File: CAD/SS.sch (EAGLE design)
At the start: 82 parts, among them Q1 SN74AHC-OR, Q2 UMD5N, Q4 SN74AHC-OR, Q5 BFP460, Q6 L78L05, Q7 NCP553, T1 MMBTRA104SS

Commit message: Board: Pouring some copper over it
Started designing the board layout.
Plus, schematic: Fixed an error on 100R relay resistor placement
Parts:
- removed C3: 27pF, aarf:MURATACAP
- removed C4, C5: 6.8pF, aarf:MURATACAP
- added L10, L11: 5.6nH, aarf:L-0805
- added L9: 56nH, aarf:L-0805
- C6: value 43pF -> 27pF
- C7: value 4.7pF -> 27pF
- L6: value 27nH -> 56nH
- L8: value 27nH -> 150nH
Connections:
- removed net N$19: C5.1, C6.2, L8.2
- removed net N$20: C5.2, L6.1
- removed net N$30: R10.2, RL2.1
- new net N$11: C7.2, L11.1, L6.1, L8.2
- new net N$8: C6.2, L10.1, L8.1, L9.2
- net GND: now also L10.2, L11.2; no longer C3.1
- net N$1: now also C17.2, D2.C
- net N$18: now also C18.1, D3.C, R10.1, RL2.1; no longer C4.2, L8.1
- net N$21: no longer C7.2
- net N$4: now also L9.1; no longer C3.2, C4.1
- net RELAY_PWR: now also R10.2; no longer C17.2, C18.1, D2.C, D3.C, R10.1
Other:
- moved on the sheet: C17, C6, C7, D2, L6, L8, R10, R9, RL1

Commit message: More copper poured
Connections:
- net N$21 renamed UHF-OUT
- net N$3 renamed VHF-IN
- net N$4 renamed UHF-IN
- net N$7 renamed VHF-OUT
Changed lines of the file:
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@@
 </segment>
 </net>
-<net name="N$21" class="0">
+<net name="UHF-OUT" class="0">
 <segment>
 <pinref part="L6" gate="G$1" pin="2"/>
@@
 </segment>
 </net>
-<net name="N$4" class="0">
+<net name="UHF-IN" class="0">
 <segment>
 <pinref part="SW_SEL_V/U-IN" gate="G$1" pin="RF2"/>
@@
 </segment>
 </net>
-<net name="N$7" class="0">
+<net name="VHF-OUT" class="0">
 <segment>
 <pinref part="SW_SEL_V/U-OUT" gate="G$1" pin="RF1"/>
@@
 </segment>
 </net>
-<net name="N$3" class="0">
+<net name="VHF-IN" class="0">
 <segment>
 <pinref part="L1" gate="G$1" pin="1"/>

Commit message: Progress
- Replaced capacitors and resistors with ones who has a PCB marking
- Poured more copper
- Added annotations
- Some block relocations
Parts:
- C13, C14, C15, C16, C17, C18, C19, C20, C21, C22, C23, C24: device rcl:C-EUC0805 -> aarf:C-0805
- R1, R10, R11, R12, R13, R14, R2, R3, R4, R5, R6, R7, R8, R9: device rcl:R-US_M1206 -> aarf:R-1206
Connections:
- net N$6 renamed IN_DECPL
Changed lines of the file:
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@@
 <part name="C7" library="aarf" deviceset="MURATACAP" device="" value="27pF"/>
 <part name="C8" library="aarf" deviceset="MURATACAP" device="" value="390pF"/>
-<part name="R1" library="rcl" library_urn="urn:adsk.eagle:library:334" deviceset="R-US_" device="M1206" package3d_urn="urn:adsk.eagle:package:23566/1" value="82kΩ"/>
-<part name="R2" library="rcl" library_urn="urn:adsk.eagle:library:334" deviceset="R-US_" device="M1206" package3d_urn="urn:adsk.eagle:package:23566/1" value="430Ω"/>
+<part name="R1" library="aarf" deviceset="R-1206" device="" value="82kΩ"/>
+<part name="R2" library="aarf" deviceset="R-1206" device="" value="430Ω"/>
 <part name="C9" library="aarf" deviceset="MURATACAP" device="" value="390pF"/>
-<part name="R3" library="rcl" library_urn="urn:adsk.eagle:library:334" deviceset="R-US_" device="M1206" package3d_urn="urn:adsk.eagle:package:23566/1" value="300Ω"/>
-<part name="R4" library="rcl" library_urn="urn:adsk.eagle:library:334" deviceset="R-US_" device="M1206" package3d_urn="urn:adsk.eagle:package:23566/1" value="130Ω"/>
+<part name="R3" library="aarf" deviceset="R-1206" device="" value="300Ω"/>
+<part name="R4" library="aarf" deviceset="R-1206" device="" value="130Ω"/>
 <part name="C10" library="aarf" deviceset="MURATACAP" device="" value="390pF"/>
 <part name="C11" library="aarf" deviceset="MURATACAP" device="" value="220nF"/>
@@
 </part>
 <part name="FB2" library="aarf" deviceset="FB-0805" device="" value="BLM21"/>
-<part name="R5" library="rcl" library_urn="urn:adsk.eagle:library:334" deviceset="R-US_" device="M1206" package3d_urn="urn:adsk.eagle:package:23566/1" value="10kΩ"/>
-<part name="C13" library="rcl" library_urn="urn:adsk.eagle:library:334" deviceset="C-EU" device="C0805" package3d_urn="urn:adsk.eagle:package:23617/2" value="0.001µ"/>
-<part name="C14" library="rcl" library_urn="urn:adsk.eagle:library:334" deviceset="C-EU" device="C0805" package3d_urn="urn:adsk.eagle:package:23617/2" value="0.001µ"/>
+<part name="R5" library="aarf" deviceset="R-1206" device="" value="10kΩ"/>
+<part name="C13" library="aarf" deviceset="C-0805" device="" value="0.001µ"/>
+<part name="C14" library="aarf" deviceset="C-0805" device="" value="0.001µ"/>
 <part name="X_8" library="ngspice-simulation" library_urn="urn:adsk.eagle:library:527439" deviceset="GND" device=""/>
-<part name="R6" library="rcl" library_urn="urn:adsk.eagle:library:334" deviceset="R-US_" device="M1206" package3d_urn="urn:adsk.eagle:package:23566/1" value="10kΩ"/>
+<part name="R6" library="aarf" deviceset="R-1206" device="" value="10kΩ"/>
 <part name="FB3" library="aarf" deviceset="FB-0805" device="" value="BLM21"/>
-<part name="C15" library="rcl" library_urn="urn:adsk.eagle:library:334" deviceset="C-EU" device="C0805" package3d_urn="urn:adsk.eagle:package:23617/2" value="0.001µ"/>
+<part name="C15" library="aarf" deviceset="C-0805" device="" value="0.001µ"/>
 <part name="Q1" library="aarf" deviceset="SN74AHC-OR" device="" package3d_urn="urn:adsk.eagle:package:2405/1"/>
-<part name="C16" library="rcl" library_urn="urn:adsk.eagle:library:334" deviceset="C-EU" device="C0805" package3d_urn="urn:adsk.eagle:package:23617/2" value="0.001µ"/>
+<part name="C16" library="aarf" deviceset="C-0805" device="" value="0.001µ"/>
 <part name="BYPASS" library="wirepad" library_urn="urn:adsk.eagle:library:412" deviceset="SMD2" device="" package3d_urn="urn:adsk.eagle:package:30839/1" value="BYPASS"/>
-<part name="R7" library="rcl" library_urn="urn:adsk.eagle:library:334" deviceset="R-US_" device="M1206" package3d_urn="urn:adsk.eagle:package:23566/1" value="10kΩ"/>
+<part name="R7" library="aarf" deviceset="R-1206" device="" value="10kΩ"/>
 <part name="FB4" library="aarf" deviceset="FB-0805" device="" value="BLM21"/>
 <part name="Q2" library="aarf" deviceset="UMD5N" device="" value="UMD5N"/>
-<part name="R9" library="rcl" library_urn="urn:adsk.eagle:library:334" deviceset="R-US_" device="M1206" package3d_urn="urn:adsk.eagle:package:23566/1" value="100Ω"/>
+<part name="R9" library="aarf" deviceset="R-1206" device="" value="100Ω"/>
 <part name="D2" library="aarf" deviceset="D-SOD323" device="" value="1N4148"/>
-<part name="C17" library="rcl" library_urn="urn:adsk.eagle:library:334" deviceset="C-EU" device="C0805" package3d_urn="urn:adsk.eagle:package:23617/2" value="0.1µ"/>
+<part name="C17" library="aarf" deviceset="C-0805" device="" value="0.1µ"/>
 <part name="D3" library="aarf" deviceset="D-SOD323" device="" value="1N4148"/>
-<part name="C18" library="rcl" library_urn="urn:adsk.eagle:library:334" deviceset="C-EU" device="C0805" package3d_urn="urn:adsk.eagle:package:23617/2" value="0.1µ"/>
-<part name="R10" library="rcl" library_urn="urn:adsk.eagle:library:334" deviceset="R-US_" device="M1206" package3d_urn="urn:adsk.eagle:package:23566/1" value="100Ω"/>
-<part name="C19" library="rcl" library_urn="urn:adsk.eagle:library:334" deviceset="C-EU" device="C0805" package3d_urn="urn:adsk.eagle:package:23617/2" value="0.001µ"/>
+<part name="C18" library="aarf" deviceset="C-0805" device="" value="0.1µ"/>
+<part name="R10" library="aarf" deviceset="R-1206" device="" value="100Ω"/>
+<part name="C19" library="aarf" deviceset="C-0805" device="" value="0.001µ"/>
 <part name="UHF" library="wirepad" library_urn="urn:adsk.eagle:library:412" deviceset="SMD2" device="" package3d_urn="urn:adsk.eagle:package:30839/1" value="UHF"/>
-<part name="R11" library="rcl" library_urn="urn:adsk.eagle:library:334" deviceset="R-US_" device="M1206" package3d_urn="urn:adsk.eagle:package:23566/1" value="10kΩ"/>
+<part name="R11" library="aarf" deviceset="R-1206" device="" value="10kΩ"/>
 <part name="FB5" library="aarf" deviceset="FB-0805" device="" value="BLM21"/>
-<part name="C20" library="rcl" library_urn="urn:adsk.eagle:library:334" deviceset="C-EU" device="C0805" package3d_urn="urn:adsk.eagle:package:23617/2" value="0.001µ"/>
+<part name="C20" library="aarf" deviceset="C-0805" device="" value="0.001µ"/>
 <part name="AMP_OFF" library="wirepad" library_urn="urn:adsk.eagle:library:412" deviceset="SMD2" device="" package3d_urn="urn:adsk.eagle:package:30839/1" value="AMP_OFF"/>
-<part name="R12" library="rcl" library_urn="urn:adsk.eagle:library:334" deviceset="R-US_" device="M1206" package3d_urn="urn:adsk.eagle:package:23566/1" value="10kΩ"/>
+<part name="R12" library="aarf" deviceset="R-1206" device="" value="10kΩ"/>
 <part name="FB6" library="aarf" deviceset="FB-0805" device="" value="BLM21"/>
 <part name="Q4" library="aarf" deviceset="SN74AHC-OR" device="" package3d_urn="urn:adsk.eagle:package:2405/1"/>
-<part name="C21" library="rcl" library_urn="urn:adsk.eagle:library:334" deviceset="C-EU" device="C0805" package3d_urn="urn:adsk.eagle:package:23617/2" value="0.33µ"/>
-<part name="C22" library="rcl" library_urn="urn:adsk.eagle:library:334" deviceset="C-EU" device="C0805" package3d_urn="urn:adsk.eagle:package:23617/2" value="0.1µ"/>
+<part name="C21" library="aarf" deviceset="C-0805" device="" value="0.33µ"/>
+<part name="C22" library="aarf" deviceset="C-0805" device="" value="0.1µ"/>
 <part name="Q7" library="aarf" deviceset="NCP553" device=""/>
-<part name="C23" library="rcl" library_urn="urn:adsk.eagle:library:334" deviceset="C-EU" device="C0805" package3d_urn="urn:adsk.eagle:package:23617/2" value="1µ"/>
-<part name="C24" library="rcl" library_urn="urn:adsk.eagle:library:334" deviceset="C-EU" device="C0805" package3d_urn="urn:adsk.eagle:package:23617/2" value="0.33µ"/>
+<part name="C23" library="aarf" deviceset="C-0805" device="" value="1µ"/>
+<part name="C24" library="aarf" deviceset="C-0805" device="" value="0.33µ"/>
 <part name="Q6" library="aarf" deviceset="MIC5365" device="" value="L78L05"/>
 <part name="SW_ISOL-ANT" library="aarf" deviceset="PE4259" device="" value="PE4259"/>
@@
 <part name="RL2" library="aarf" deviceset="RELAY-TE-HF3" device="" value="RADIO_RLY"/>
 <part name="T1" library="transistor" library_urn="urn:adsk.eagle:library:402" deviceset="*-PNP_DRIVER-" device="SC59-BEC" package3d_urn="urn:adsk.eagle:package:28754/2" technology="MUN2111T1" value="MMBTRA104SS"/>
-<part name="R8" library="rcl" library_urn="urn:adsk.eagle:library:334" deviceset="R-US_" device="M1206" package3d_urn="urn:adsk.eagle:package:23566/1" value="1kΩ"/>
+<part name="R8" library="aarf" deviceset="R-1206" device="" value="1kΩ"/>
 <part name="L7" library="aarf" deviceset="L-0805" device="" value="1000µH"/>
-<part name="R13" library="rcl" library_urn="urn:adsk.eagle:library:334" deviceset="R-US_" device="M1206" package3d_urn="urn:adsk.eagle:package:23566/1" value="10kΩ"/>
-<part name="R14" library="rcl" library_urn="urn:adsk.eagle:library:334" deviceset="R-US_" device="M1206" package3d_urn="urn:adsk.eagle:package:23566/1" value="10kΩ"/>
+<part name="R13" library="aarf" deviceset="R-1206" device="" value="10kΩ"/>
+<part name="R14" library="aarf" deviceset="R-1206" device="" value="10kΩ"/>
 <part name="ANTENNA" library="wirepad" library_urn="urn:adsk.eagle:library:412" deviceset="SMD2" device="" package3d_urn="urn:adsk.eagle:package:30839/1" value="ANTENNA"/>
 <part name="RADIO" library="wirepad" library_urn="urn:adsk.eagle:library:412" deviceset="SMD2" device="" package3d_urn="urn:adsk.eagle:package:30839/1" value="RADIO"/>
@@
 </segment>
 </net>
-<net name="N$6" class="0">
+<net name="IN_DECPL" class="0">
 <segment>
 <pinref part="C25" gate="G$1" pin="2"/>
@@
 packages will not be understood (or retained) with this version.
 </note>
-<note version="8.4" severity="warning">
-Since Version 8.4, EAGLE supports properties for SPICE simulation.
-Probes in schematics and SPICE mapping objects found in parts and library devices
-will not be understood with this version. Update EAGLE to the latest version
-for full support of SPICE simulation.
-</note>
 </compatibility>

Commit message: More progress
- Featuring: CPWs (check https://resources.altium.com/p/pros-and-cons-of-different-high-frequency-transmission-line-types)
- Revamped BPF component layout
- Serious routing in RF side
- More labeled signals

Getting closer to the real deal
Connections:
- net N$1 renamed FEED-RA
- net N$18 renamed FEED-RB
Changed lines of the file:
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@@
 </segment>
 </net>
-<net name="N$18" class="0">
+<net name="FEED-RB" class="0">
 <segment>
 <wire x1="307.34" y1="228.6" x2="307.34" y2="243.84" width="0.1524" layer="91"/>
@@
 </segment>
 </net>
-<net name="N$1" class="0">
+<net name="FEED-RA" class="0">
 <segment>
 <pinref part="R9" gate="G$1" pin="2"/>

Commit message: Fixed crass error on LNA RF switch
it was flipped the ports RF1/RF2 (NO/NC)
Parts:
- VHF: value UHF -> VHF
- renumbered UHF to VHF
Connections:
- net SEL_BPF_UHF renamed SEL_BPF_VHF
- removed net LNA_BYPASS: SW_SEL_LNA-IN.RF2, SW_SEL_LNA-OUT.RF2
- removed net LNA_IN: C8.1, SW_SEL_LNA-IN.RF1
- removed net LNA_OUT: C12.2, SW_SEL_LNA-OUT.RF1
- new net LNA-BYPASS: SW_SEL_LNA-IN.NO, SW_SEL_LNA-OUT.NO
- new net N$1: C12.2, SW_SEL_LNA-OUT.NC
- new net N$4: C8.1, SW_SEL_LNA-IN.NC
- net BPF_IN: now also SW_ISOL-ANT.NC; no longer SW_ISOL-ANT.RF2
- net GND: now also SW_ISOL-ANT.NO, SW_ISOL-RADIO.NO; no longer SW_ISOL-ANT.RF1, SW_ISOL-RADIO.RF1
- net LNA-SW_OUT: now also SW_ISOL-RADIO.NC; no longer SW_ISOL-RADIO.RF2
- net UHF-IN: now also SW_SEL_V/U-IN.NC; no longer SW_SEL_V/U-IN.RF2
- net UHF-OUT: now also SW_SEL_V/U-OUT.NC; no longer SW_SEL_V/U-OUT.RF2
- net VHF-IN: now also SW_SEL_V/U-IN.NO; no longer SW_SEL_V/U-IN.RF1
- net VHF-OUT: now also SW_SEL_V/U-OUT.NO; no longer SW_SEL_V/U-OUT.RF1
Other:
- moved on the sheet: D4, SW_ISOL-RADIO, SW_SEL_LNA-IN, SW_SEL_LNA-OUT

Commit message: Fixed relay/switch logics
* REviewed thoroughly the relay logic and connectors.
* Had to add a new "NOR" part. Complexity wins...
* Re-routed 5V regulator Enable pin to LNA logic
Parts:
- AMP_ON: value AMP_OFF -> AMP_ON
- Q1: value SN74AHC-OR -> SN74AHC-NOR; device aarf:SN74AHC-OR -> aarf:SN74AHC-NOR
- Q4: value SN74AHC-OR -> SN74AHC-AND; device aarf:SN74AHC-OR -> aarf:SN74AHC-AND
- renumbered AMP_OFF to AMP_ON
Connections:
- net AMP_OFF renamed AMP_ON
- net EXT_BYPASS renamed FORCE_BYPASS
- net RELAY_PWR renamed RELAY-RX_ON
- removed net LNA_OFF: Q4.Y, SW_SEL_LNA-IN.CTRL, SW_SEL_LNA-OUT.CTRL
- removed net N$4: C8.1, SW_SEL_LNA-IN.NC
- removed net RLY_BYPASS: Q1.Y, Q2.5, Q4.A, Q6.EN, SW_ISOL-ANT.CTRL, SW_ISOL-RADIO.CTRL
- new net BPF_ON: Q1.Y, Q2.5, Q4.A, SW_ISOL-ANT.CTRL, SW_ISOL-RADIO.CTRL
- new net LNA_ON: Q4.Y, Q6.EN, SW_SEL_LNA-IN.CTRL, SW_SEL_LNA-OUT.CTRL
- new net N$3: C8.1, SW_SEL_LNA-IN.NO
- net BPF_IN: now also SW_ISOL-ANT.NO; no longer SW_ISOL-ANT.NC
- net GND: now also SW_ISOL-ANT.NC, SW_ISOL-RADIO.NC; no longer SW_ISOL-ANT.NO, SW_ISOL-RADIO.NO
- net LNA-BYPASS: now also SW_SEL_LNA-IN.NC, SW_SEL_LNA-OUT.NC; no longer SW_SEL_LNA-IN.NO, SW_SEL_LNA-OUT.NO
- net LNA-SW_OUT: now also SW_ISOL-RADIO.NO; no longer SW_ISOL-RADIO.NC
- net N$1: now also SW_SEL_LNA-OUT.NO; no longer SW_SEL_LNA-OUT.NC
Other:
- note added: "LNA CONTROL"
- note removed: "LNA CONTROL ON/BYP"
- moved on the sheet: SW_SEL_LNA-IN, SW_SEL_LNA-OUT

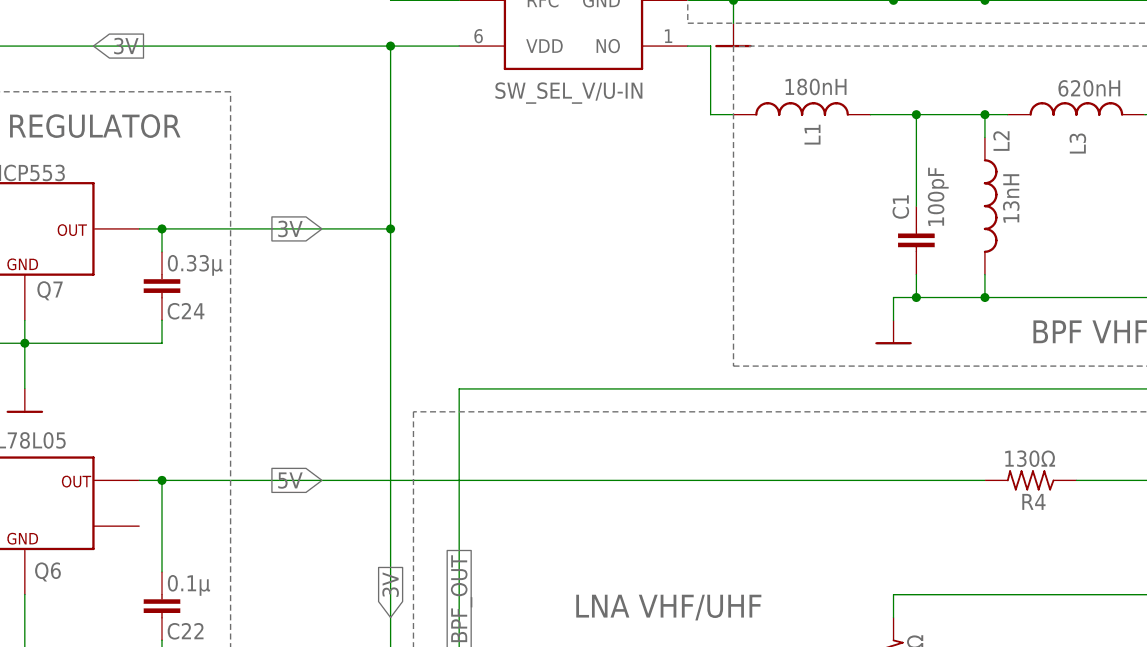
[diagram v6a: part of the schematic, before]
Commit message: Updates to Board & Schematics
Schematic: 
* Added pads for 3V and 5V
Board:
* Added signal direction on signal pads
* Added a lot of gimmicks
* Added exposed copper so I can try the effects of covering some RF-critical sections with copper tape
* Reviewed some component position
* More comments
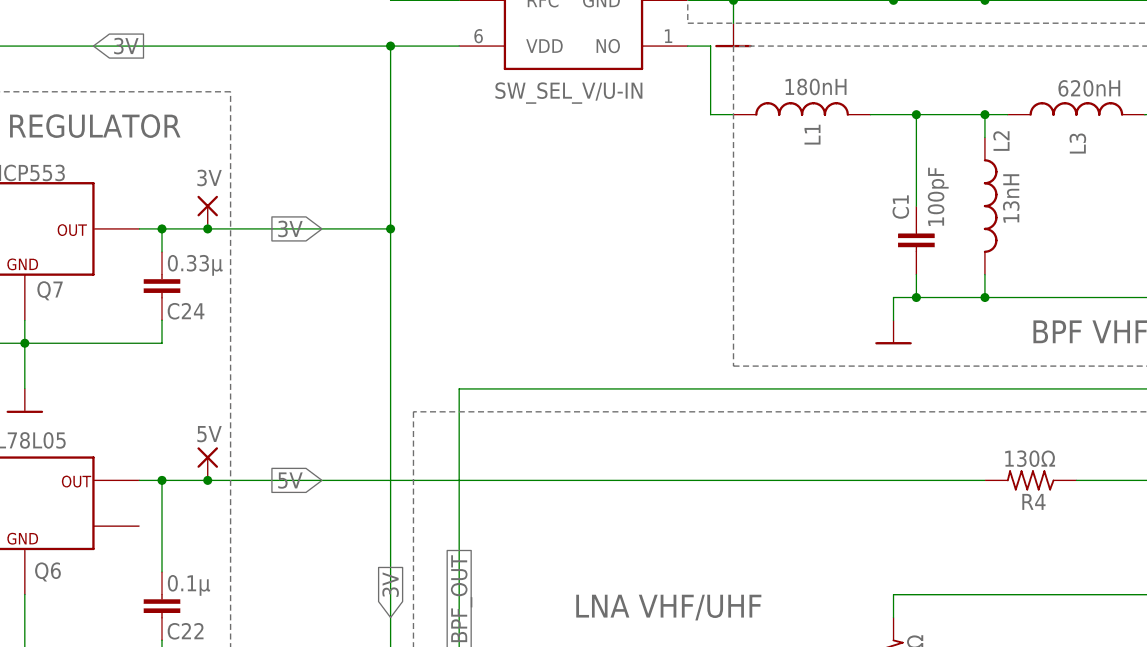
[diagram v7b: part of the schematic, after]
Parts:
- added 3V: 3V, wirepad:SMD2
- added 5V: 5V, wirepad:SMD2
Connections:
- net 3V: now also 3V.P
- net 5V: now also 5V.P
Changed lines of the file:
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@@
 <part name="GND16" library="supply1" library_urn="urn:adsk.eagle:library:371" deviceset="GND" device=""/>
 <part name="GND18" library="supply1" library_urn="urn:adsk.eagle:library:371" deviceset="GND" device=""/>
+<part name="5V" library="wirepad" library_urn="urn:adsk.eagle:library:412" deviceset="SMD2" device="" package3d_urn="urn:adsk.eagle:package:30839/1" value="5V"/>
+<part name="3V" library="wirepad" library_urn="urn:adsk.eagle:library:412" deviceset="SMD2" device="" package3d_urn="urn:adsk.eagle:package:30839/1" value="3V"/>
 </parts>
 <sheets>
@@
 <instance part="GND16" gate="1" x="281.94" y="58.42" smashed="yes"/>
 <instance part="GND18" gate="1" x="210.82" y="58.42" smashed="yes"/>
+<instance part="5V" gate="1" x="149.86" y="114.3" smashed="yes" rot="R270">
+<attribute name="NAME" x="149.987" y="116.9162" size="1.778" layer="95" align="center"/>
+</instance>
+<instance part="3V" gate="1" x="149.86" y="142.24" smashed="yes" rot="R270">
+<attribute name="NAME" x="149.987" y="145.3642" size="1.778" layer="95" align="center"/>
+</instance>
 </instances>
 <busses>
@@
 <pinref part="C22" gate="G$1" pin="2"/>
 <wire x1="144.78" y1="111.76" x2="144.78" y2="101.6" width="0.1524" layer="91"/>
-<wire x1="144.78" y1="111.76" x2="236.22" y2="111.76" width="0.1524" layer="91"/>
+<wire x1="144.78" y1="111.76" x2="149.86" y2="111.76" width="0.1524" layer="91"/>
 <junction x="144.78" y="111.76"/>
 <pinref part="R4" gate="G$1" pin="2"/>
 <label x="162.56" y="111.76" size="1.778" layer="255" rot="R180" xref="yes"/>
 <pinref part="Q6" gate="G$1" pin="VOUT"/>
+<pinref part="5V" gate="1" pin="P"/>
+<wire x1="149.86" y1="111.76" x2="236.22" y2="111.76" width="0.1524" layer="91"/>
+<junction x="149.86" y="111.76"/>
 </segment>
 </net>
@@
 <wire x1="170.18" y1="160.02" x2="119.38" y2="160.02" width="0.1524" layer="91"/>
 <junction x="170.18" y="160.02"/>
-<wire x1="144.78" y1="139.7" x2="170.18" y2="139.7" width="0.1524" layer="91"/>
+<wire x1="144.78" y1="139.7" x2="149.86" y2="139.7" width="0.1524" layer="91"/>
 <junction x="144.78" y="139.7"/>
 <junction x="170.18" y="139.7"/>
 <label x="162.56" y="139.7" size="1.778" layer="255" rot="R180" xref="yes"/>
 <pinref part="SW_ISOL-ANT" gate="G$1" pin="VDD"/>
+<wire x1="149.86" y1="139.7" x2="170.18" y2="139.7" width="0.1524" layer="91"/>
 <wire x1="132.08" y1="193.04" x2="119.38" y2="193.04" width="0.1524" layer="91"/>
 <wire x1="119.38" y1="193.04" x2="119.38" y2="160.02" width="0.1524" layer="91"/>
@@
 <wire x1="180.34" y1="73.66" x2="180.34" y2="83.82" width="0.1524" layer="91"/>
 <wire x1="180.34" y1="83.82" x2="170.18" y2="83.82" width="0.1524" layer="91"/>
-</segment>
-</net>
+<pinref part="3V" gate="1" pin="P"/>
+<junction x="149.86" y="139.7"/>
+</segment>
+</net>
